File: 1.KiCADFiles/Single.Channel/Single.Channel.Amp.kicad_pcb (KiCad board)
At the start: 2 copper layers, 50 x 43.8 mm, 20 parts

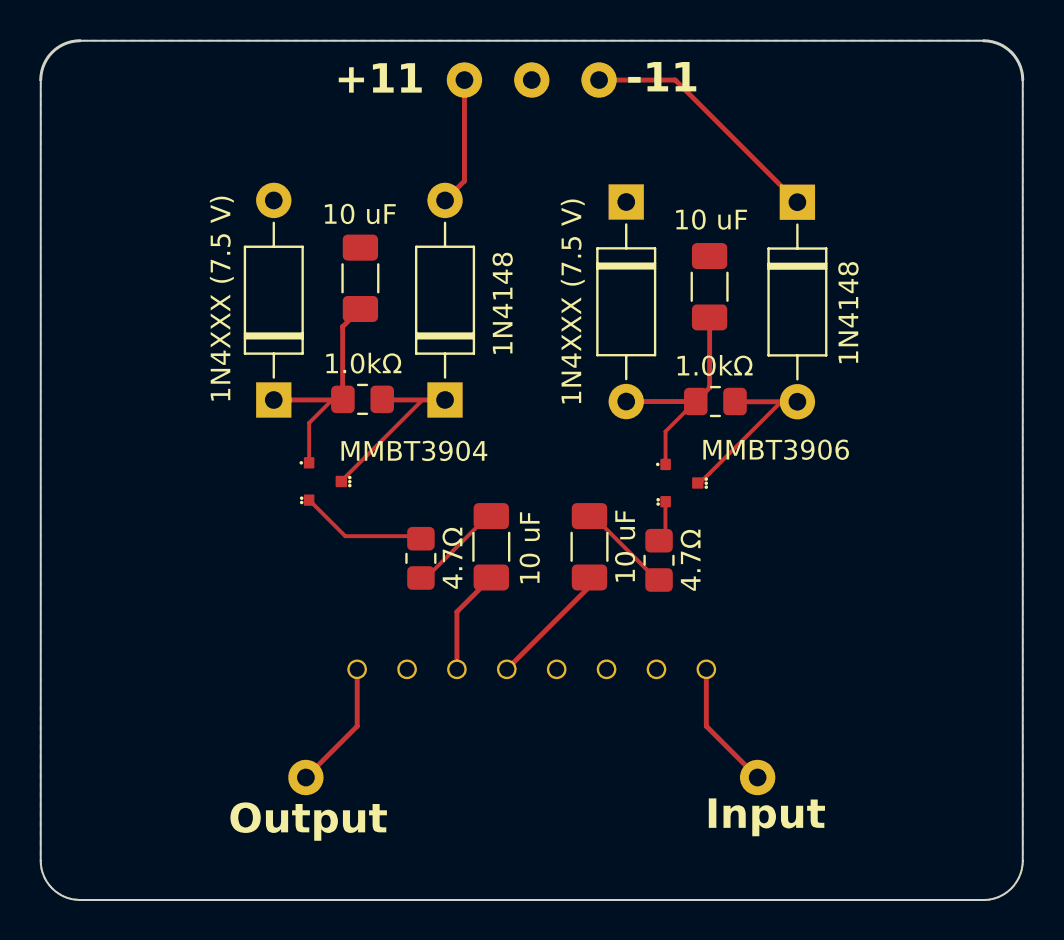
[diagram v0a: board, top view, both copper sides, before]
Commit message: Small Adjustments to Single Channel
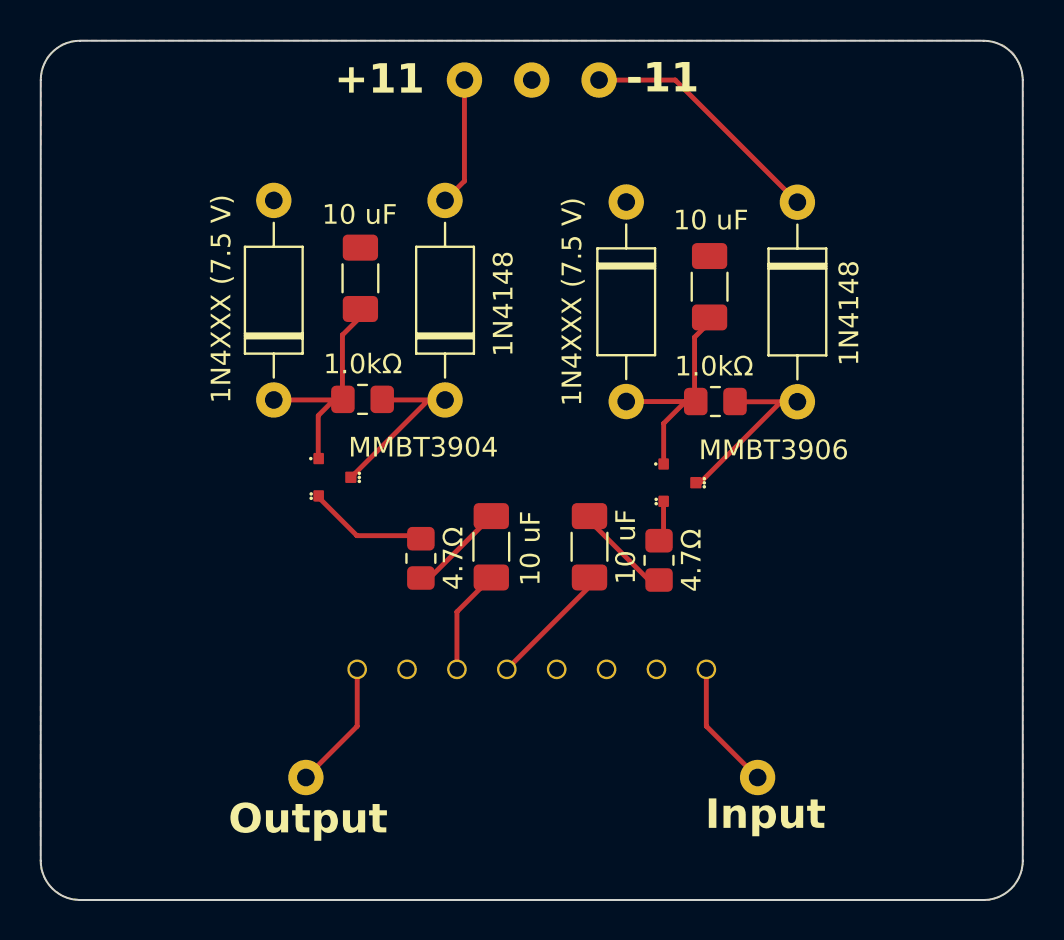
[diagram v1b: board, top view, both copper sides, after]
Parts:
- moved MMBT3904 0.53 mm to (39.1, 42.8)
- moved MMBT3906 0.10 mm to (56.6, 43.0)

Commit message: Minor Changes
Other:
- board text added: "Single Channel Amp v.1 June 2023 Alfredo Barajas Enriquez"
- board text removed: "June 2023 Alfredo Barajas Enriquez"
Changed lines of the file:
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@@
   (gr_circle (center 53.111459 22.545) (end 53.361459 22.545)
     (stroke (width 0.15) (type default)) (fill none) (layer "User.8"))
-  (gr_text "June 2023\nAlfredo Barajas Enriquez\n" (at 63.515 47.975) (layer "B.SilkS")
+  (gr_text "Single Channel Amp v.1\nJune 2023\nAlfredo Barajas Enriquez\n" (at 64.25 48.4) (layer "B.SilkS")
     (effects (font (size 1.5 1.5) (thickness 0.25) bold) (justify left bottom mirror))
   )
